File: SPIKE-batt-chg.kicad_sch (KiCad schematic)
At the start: 18 parts, among them IC1 CH224K, J1 USB_C_Receptacle_USB2.0, J2 Barrel_Jack_Switch, Q1 PMOS

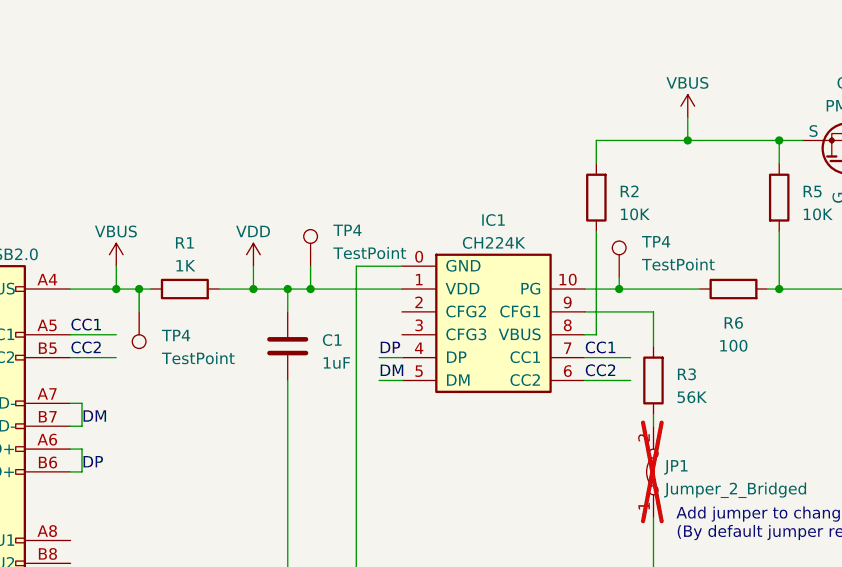
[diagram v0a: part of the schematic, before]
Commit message: Fix the routing for rotated MOSFET
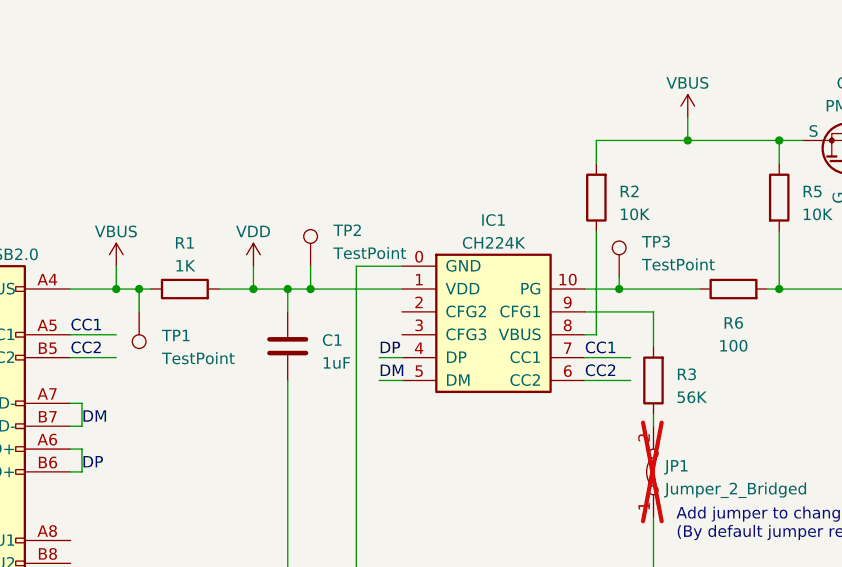
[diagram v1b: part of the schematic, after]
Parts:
- renumbered TP4 to TP1, TP4 to TP2, TP4 to TP3
